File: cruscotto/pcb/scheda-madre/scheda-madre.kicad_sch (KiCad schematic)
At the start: 47 parts, among them J1 Micro-Fit 43045-2400 (D-044), Q1 IPD50N06S4L-12 (60V, da confe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, U1 LM74700-Q1, U2 TPS54360B, U3 LMR36510

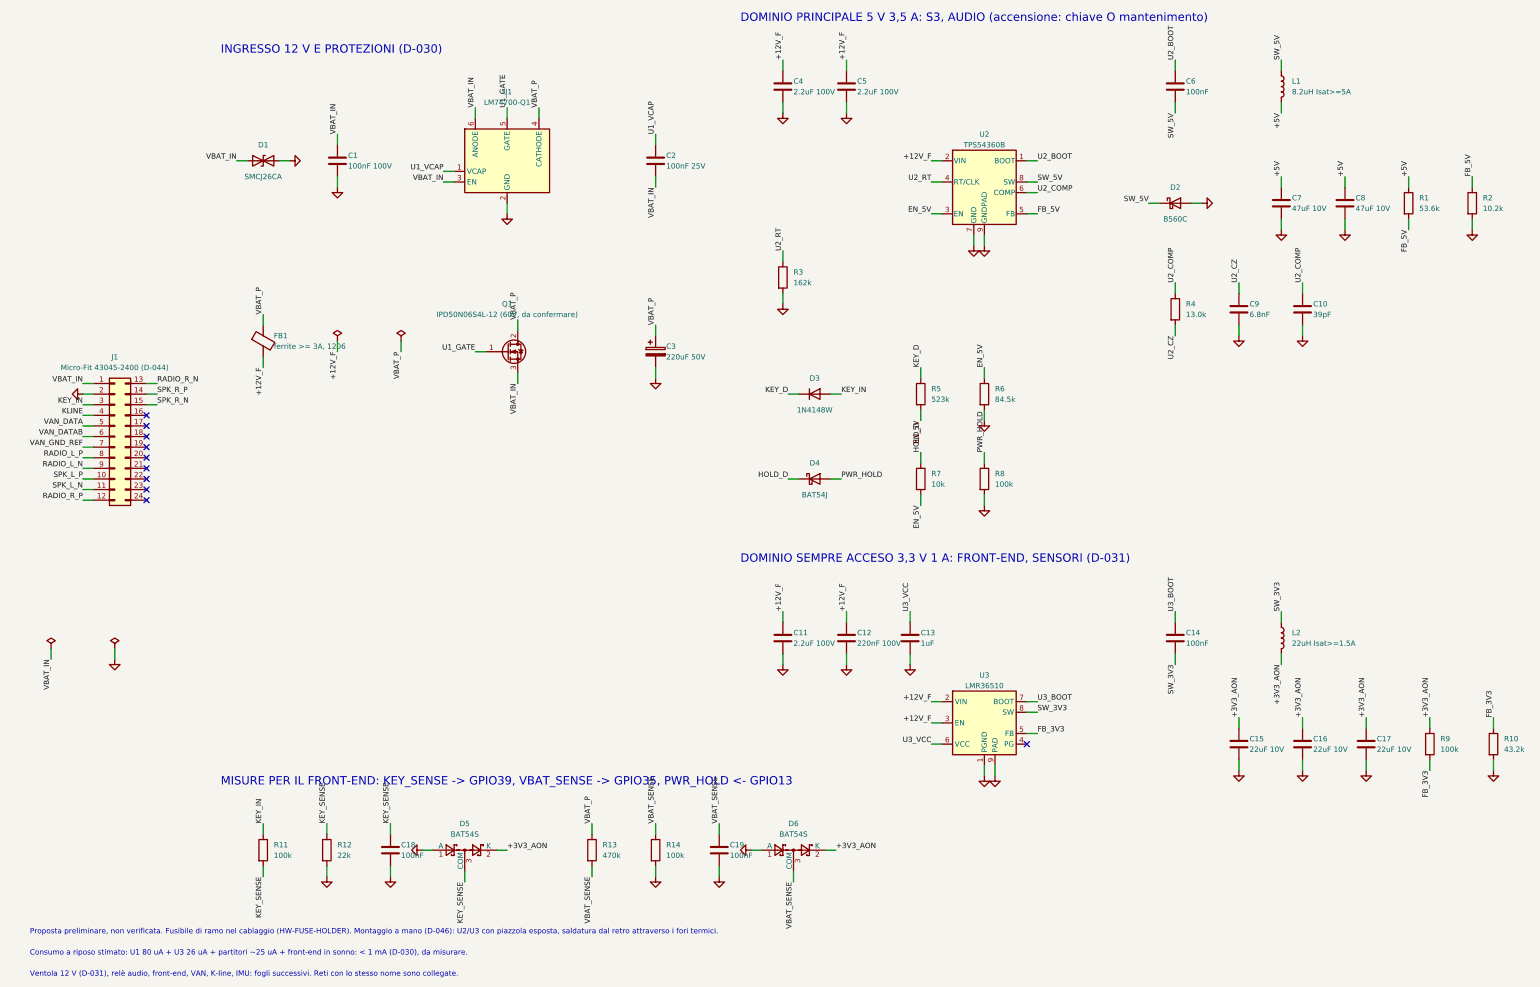
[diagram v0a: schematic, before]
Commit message: feat(schematic): CR-EL-001 rev B with drawn wires inside each block
Labels only for nets leaving a block; the generator checks the KiCad netlist against the intended nets. ERC: 0 errors, 12 expected warnings.

Co-Authored-By: Claude Opus 5.5 <noreply@anthropic.com>
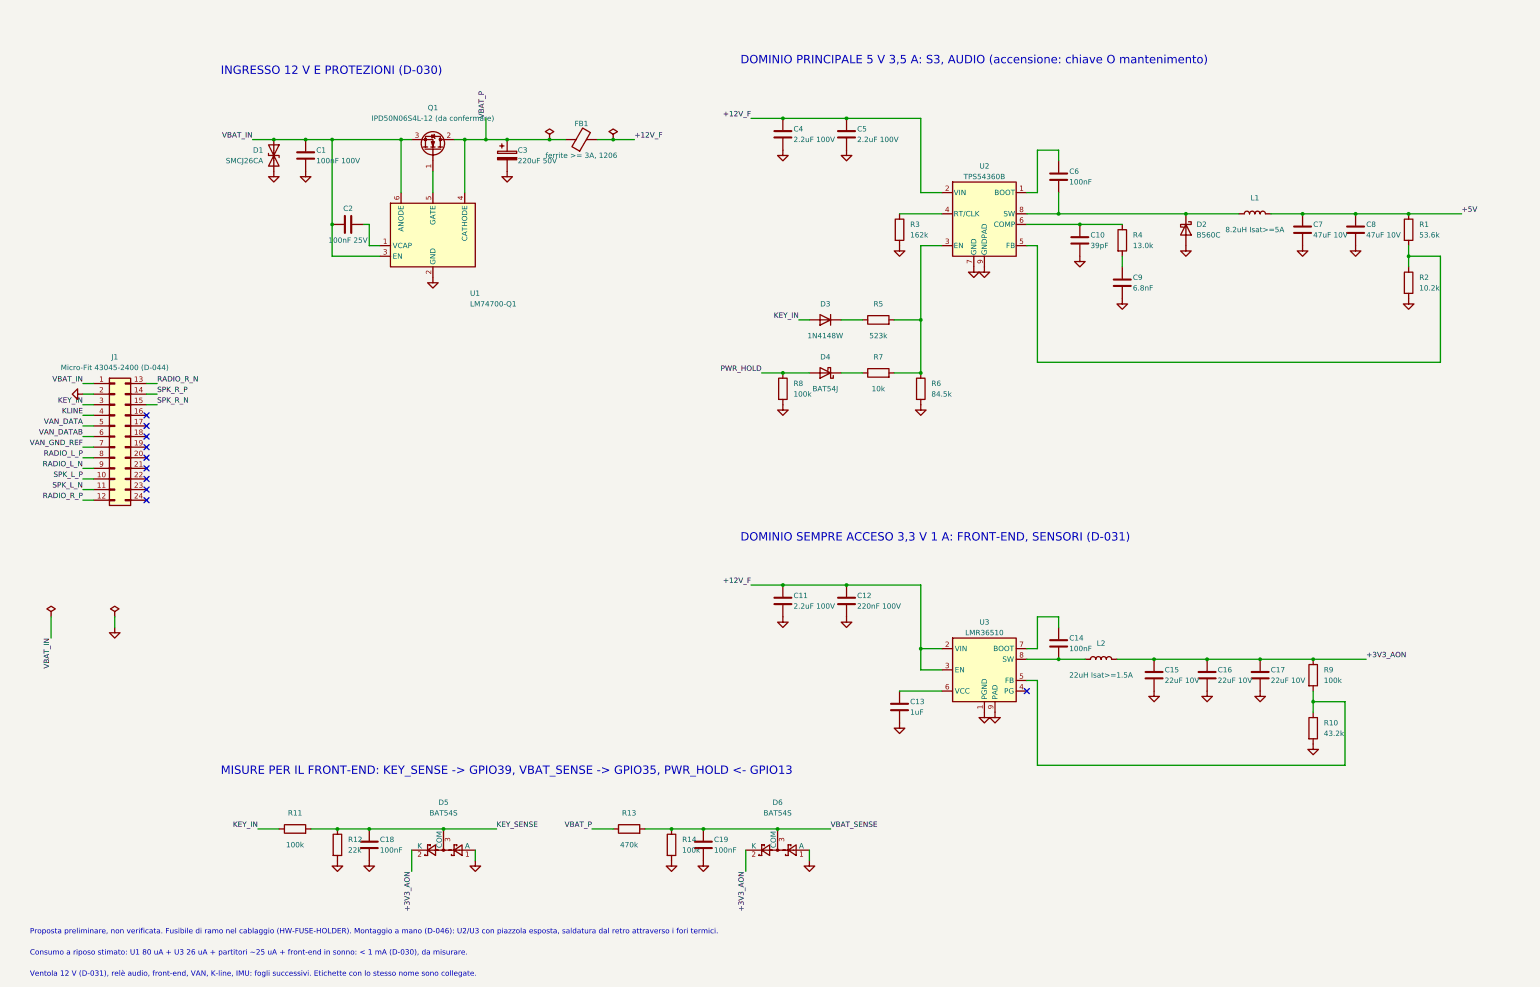
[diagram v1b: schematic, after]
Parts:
- Q1: value IPD50N06S4L-12 (60V, da confermare) -> IPD50N06S4L-12 (da confermare)
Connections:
- net VBAT_IN: now also C2.1; no longer C2.2
- net EN_5V: no longer names the net of R5.2, R6.1, R7.2, U2.3 (EN)
- net FB_3V3: no longer names the net of R10.1, R9.2, U3.5 (FB)
- net FB_5V: no longer names the net of R1.2, R2.1, U2.5 (FB)
- net HOLD_D: no longer names the net of D4.1 (K), R7.1
- net KEY_D: no longer names the net of D3.1 (K), R5.1
- net SW_3V3: no longer names the net of C14.2, L2.1, U3.8 (SW)
- net SW_5V: no longer names the net of C6.2, D2.1 (K), L1.1, U2.8 (SW)
- net U1_GATE: no longer names the net of Q1.1 (G), U1.5 (GATE)
- net U1_VCAP: no longer names the net of U1.1 (VCAP)
- net U1_VCAP: now also C2.2; no longer C2.1
- net U2_BOOT: no longer names the net of C6.1, U2.1 (BOOT)
- net U2_COMP: no longer names the net of C10.1, R4.1, U2.6 (COMP)
- net U2_CZ: no longer names the net of C9.1, R4.2
- net U2_RT: no longer names the net of R3.1, U2.4 (RT/CLK)
- net U3_BOOT: no longer names the net of C14.1, U3.7 (BOOT)
- net U3_VCC: no longer names the net of C13.1, U3.6 (VCC)
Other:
- note added: "Ventola 12 V (D-031), relè audio, front-end, VAN, K-line, IMU: fogli successivi. Etichette con lo stesso nome sono collegate."
- note removed: "Ventola 12 V (D-031), relè audio, front-end, VAN, K-line, IMU: fogli successivi. Reti con lo stesso nome sono collegate."
- moved on the sheet: C1, C10, C11, C12, C13, C14, C15, C16, C17, C18, C19, C2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

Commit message: feat(schematic): front-end sheet C3AI-CR-EL-002 rev A; power sheet rev C as hierarchical root
ESP32-WROOM-32E with bench-only USB-C + CH340C (USB powered), auto-reset, link to the S3, I2C pull-ups, two 100k NTCs, 4-wire fan with high-side switch on GPIO2. Global labels across sheets; the generator checks 81 nets against the KiCad netlist. Inventory: open conflict on factory vs hand mounting of HW-FE-MODULE (D-046).

Co-Authored-By: Claude Opus 5.5 <noreply@anthropic.com>
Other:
- added sheet Front-end (front-end.kicad_sch)

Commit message: feat(schematic): vehicle interface sheet C3AI-CR-EL-003 rev A (K-line and receive-only VAN)
K-line from KL-001 rev F with TVS, series diode and key-referenced threshold; SN65HVD230 receive-only with NUP2105L and its own switched 3.3 V. Generator supports multi-unit symbols and rejects zero-length wires. ERC: 0 errors, 15 expected warnings; 88 nets checked against the KiCad netlist.

Co-Authored-By: Claude Opus 5.5 <noreply@anthropic.com>
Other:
- added sheet Interfacce veicolo (interfacce-veicolo.kicad_sch)
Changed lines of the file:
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@@
 		(instances (project "scheda-madre" (path "/ccee1fe6-cbff-5665-be3b-629f18d22eb3" (page "2"))))
+	)
+	(sheet (at 20.32 213.36) (size 38.1 15.24) (exclude_from_sim no) (in_bom yes) (on_board yes) (dnp no) (stroke (width 0.1524) (type solid)) (fill (color 0 0 0 0.0000))
+		(property "Sheetname" "Interfacce veicolo" (at 20.32 212.66 0) (effects (font (size 1.27 1.27)) (justify left bottom)))
+		(property "Sheetfile" "interfacce-veicolo.kicad_sch" (at 20.32 229.2 0) (effects (font (size 1.27 1.27)) (justify left top)))
+		(instances (project "scheda-madre" (path "/ccee1fe6-cbff-5665-be3b-629f18d22eb3" (page "3"))))
 	)
 	(symbol (lib_id "Connector_Generic:Conn_02x12_Top_Bottom") (at 45.72 116.84 0) (unit 1) (exclude_from_sim no) (in_bom yes) (on_board yes) (dnp no)

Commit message: feat(schematic): sensors and memory sheet C3AI-CR-EL-004 rev A
DIL-24 socket for the STEVAL-MKI196V1 IMU module (I2C 0x6A), optional DS3231SN RTC with non-recharged CR2032, optional MicroSD on the logger SPI pins with pull-ups and switched 3.3 V. Sheet boxes moved to the free area of the root. ERC: 0 errors, 11 expected warnings; 91 nets checked.

Co-Authored-By: Claude Opus 5.5 <noreply@anthropic.com>
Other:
- added sheet Sensori e memoria (sensori-memoria.kicad_sch)
- note added: "Sottofogli: front-end, interfacce veicolo, sensori e memoria. Collegamento con l’S3 e relè audio: da disegnare dopo il rilievo dei connettori della S3. Etichette con lo stesso nome sono collegate."
- note removed: "Ventola 12 V (D-031), relè audio, front-end, VAN, K-line, IMU: fogli successivi. Etichette con lo stesso nome sono collegate."
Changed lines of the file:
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@@
 		(comment 3 "Generato da tools/genera-schema-scheda-madre.py")
 	)
-	(sheet (at 20.32 187.96) (size 38.1 15.24) (exclude_from_sim no) (in_bom yes) (on_board yes) (dnp no) (stroke (width 0.1524) (type solid)) (fill (color 0 0 0 0.0000))
-		(property "Sheetname" "Front-end" (at 20.32 187.26 0) (effects (font (size 1.27 1.27)) (justify left bottom)))
-		(property "Sheetfile" "front-end.kicad_sch" (at 20.32 203.8 0) (effects (font (size 1.27 1.27)) (justify left top)))
+	(sheet (at 279.4 205.74) (size 38.1 12.7) (exclude_from_sim no) (in_bom yes) (on_board yes) (dnp no) (stroke (width 0.1524) (type solid)) (fill (color 0 0 0 0.0000))
+		(property "Sheetname" "Front-end" (at 279.4 205.04 0) (effects (font (size 1.27 1.27)) (justify left bottom)))
+		(property "Sheetfile" "front-end.kicad_sch" (at 279.4 219.04 0) (effects (font (size 1.27 1.27)) (justify left top)))
 		(instances (project "scheda-madre" (path "/ccee1fe6-cbff-5665-be3b-629f18d22eb3" (page "2"))))
 	)
-	(sheet (at 20.32 213.36) (size 38.1 15.24) (exclude_from_sim no) (in_bom yes) (on_board yes) (dnp no) (stroke (width 0.1524) (type solid)) (fill (color 0 0 0 0.0000))
-		(property "Sheetname" "Interfacce veicolo" (at 20.32 212.66 0) (effects (font (size 1.27 1.27)) (justify left bottom)))
-		(property "Sheetfile" "interfacce-veicolo.kicad_sch" (at 20.32 229.2 0) (effects (font (size 1.27 1.27)) (justify left top)))
+	(sheet (at 279.4 228.6) (size 38.1 12.7) (exclude_from_sim no) (in_bom yes) (on_board yes) (dnp no) (stroke (width 0.1524) (type solid)) (fill (color 0 0 0 0.0000))
+		(property "Sheetname" "Interfacce veicolo" (at 279.4 227.9 0) (effects (font (size 1.27 1.27)) (justify left bottom)))
+		(property "Sheetfile" "interfacce-veicolo.kicad_sch" (at 279.4 241.9 0) (effects (font (size 1.27 1.27)) (justify left top)))
 		(instances (project "scheda-madre" (path "/ccee1fe6-cbff-5665-be3b-629f18d22eb3" (page "3"))))
+	)
+	(sheet (at 332.74 205.74) (size 38.1 12.7) (exclude_from_sim no) (in_bom yes) (on_board yes) (dnp no) (stroke (width 0.1524) (type solid)) (fill (color 0 0 0 0.0000))
+		(property "Sheetname" "Sensori e memoria" (at 332.74 205.04 0) (effects (font (size 1.27 1.27)) (justify left bottom)))
+		(property "Sheetfile" "sensori-memoria.kicad_sch" (at 332.74 219.04 0) (effects (font (size 1.27 1.27)) (justify left top)))
+		(instances (project "scheda-madre" (path "/ccee1fe6-cbff-5665-be3b-629f18d22eb3" (page "4"))))
 	)
 	(symbol (lib_id "Connector_Generic:Conn_02x12_Top_Bottom") (at 45.72 116.84 0) (unit 1) (exclude_from_sim no) (in_bom yes) (on_board yes) (dnp no)
@@
 	(text "Proposta preliminare, non verificata. Fusibile di ramo nel cablaggio (HW-FUSE-HOLDER). Montaggio a mano (D-046): U2/U3 con piazzola esposta, saldatura dal retro attraverso i fori termici." (exclude_from_sim no) (at 25.4 236.22 0) (effects (font (size 1.27 1.27)) (justify left bottom)))
 	(text "Consumo a riposo stimato: U1 80 uA + U3 26 uA + partitori ~25 uA + front-end in sonno: < 1 mA (D-030), da misurare." (exclude_from_sim no) (at 25.4 241.3 0) (effects (font (size 1.27 1.27)) (justify left bottom)))
-	(text "Ventola 12 V (D-031), relè audio, front-end, VAN, K-line, IMU: fogli successivi. Etichette con lo stesso nome sono collegate." (exclude_from_sim no) (at 25.4 246.38 0) (effects (font (size 1.27 1.27)) (justify left bottom)))
+	(text "Sottofogli: front-end, interfacce veicolo, sensori e memoria. Collegamento con l’S3 e relè audio: da disegnare dopo il rilievo dei connettori della S3. Etichette con lo stesso nome sono collegate." (exclude_from_sim no) (at 25.4 246.38 0) (effects (font (size 1.27 1.27)) (justify left bottom)))
 	(junction (at 83.82 45.72) (diameter 0) (color 0 0 0 0))
 	(junction (at 91.44 45.72) (diameter 0) (color 0 0 0 0))

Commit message: feat(schematic): S3 link and audio relay sheet C3AI-CR-EL-005 rev A; schematic complete in five sheets
MX1.25 cables to S3 P1/P2/P6 with Schottky on the 5 V feed; two G2RL-2 relays driven by AO3400A from S3 IO13, speakers in series on the S3 output when energised, radio restored at rest. Inventory: S3 connector order, MX1.25 plugs. ERC: 0 errors, 1 warning (VAN ground reference); 95 nets checked.

Co-Authored-By: Claude Opus 5.5 <noreply@anthropic.com>
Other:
- added sheet Collegamento S3 e audio (s3-audio.kicad_sch)
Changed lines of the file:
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@@
 		(instances (project "scheda-madre" (path "/ccee1fe6-cbff-5665-be3b-629f18d22eb3" (page "4"))))
+	)
+	(sheet (at 332.74 228.6) (size 38.1 12.7) (exclude_from_sim no) (in_bom yes) (on_board yes) (dnp no) (stroke (width 0.1524) (type solid)) (fill (color 0 0 0 0.0000))
+		(property "Sheetname" "Collegamento S3 e audio" (at 332.74 227.9 0) (effects (font (size 1.27 1.27)) (justify left bottom)))
+		(property "Sheetfile" "s3-audio.kicad_sch" (at 332.74 241.9 0) (effects (font (size 1.27 1.27)) (justify left top)))
+		(instances (project "scheda-madre" (path "/ccee1fe6-cbff-5665-be3b-629f18d22eb3" (page "5"))))
 	)
 	(symbol (lib_id "Connector_Generic:Conn_02x12_Top_Bottom") (at 45.72 116.84 0) (unit 1) (exclude_from_sim no) (in_bom yes) (on_board yes) (dnp no)

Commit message: feat(bom): power parts verified (Q1, L1, L2, C3), complete purchase list per supplier
- Verification 28/10/2026 from DigiKey parameters and TI pages: IPD50N06S4L-12 (0.06 W at 2.2 A,
  LM74700 gate 12.1-13 V below VGS 16 V), SRR1260-8R2Y (Isat 5.8 A, peak 2.45 A at 2 A load),
  SRN6045TA-220M (Isat 3.3 A, peak 1.17 A), EEU-FR1H221 (about 1 ms ride-through; 17.5 mm tall:
  mount lying down). Schematic EL-001 rev D values and notes, board values updated; DRC unchanged
  (0 errors, 0 unconnected).
- lista-acquisti-scheda-madre.md: LCSC cart (55 lines, 84.52 USD + 13 USD shipping), Farnell quick
  order (16 lines incl. second STEVAL and Micro-Fit bench plug), DigiKey L1 and fan, second MicroSD
  and VAN modules, PCB after Gerbers.

Co-Authored-By: Claude Opus 5.5 <noreply@anthropic.com>
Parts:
- L1: value 8.2uH Isat>=5A -> SRR1260-8R2Y
- L2: value 22uH Isat>=1.5A -> SRN6045TA-220M
- Q1: value IPD50N06S4L-12 (da confermare) -> IPD50N06S4L-12
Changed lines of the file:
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@@
 	(title_block
 		(title "Scheda madre cruscotto C3+AI - alimentazione")
-		(date "2026-10-24")
-		(rev "C")
+		(date "2026-10-28")
+		(rev "D")
 		(company "Cruscotto C3+AI")
-		(comment 1 "C3AI-CR-EL-001 rev C - proposta preliminare, non verificata")
+		(comment 1 "C3AI-CR-EL-001 rev D - proposta preliminare, non verificata")
 		(comment 2 "D-030, D-031, D-044, D-046, D-047, D-048")
 		(comment 3 "Generato da tools/genera-schema-scheda-madre.py")
@@
 	(symbol (lib_id "Transistor_FET:IPD50R380CE") (at 121.92 48.26 90) (mirror y) (unit 1) (exclude_from_sim no) (in_bom yes) (on_board yes) (dnp no)
 		(property "Reference" "Q1" (at 121.92 38.1 90) (effects (font (size 1.27 1.27))))
-		(property "Value" "IPD50N06S4L-12 (da confermare)" (at 121.92 40.64 90) (effects (font (size 1.27 1.27))))
+		(property "Value" "IPD50N06S4L-12" (at 121.92 40.64 90) (effects (font (size 1.27 1.27))))
 		(property "Footprint" "Package_TO_SOT_SMD:TO-252-2" (at 121.92 48.26 0) (hide yes) (effects (font (size 1.27 1.27))))
 		(property "Datasheet" "" (at 121.92 48.26 0) (hide yes) (effects (font (size 1.27 1.27))))
@@
 		(property "Footprint" "Capacitor_THT:CP_Radial_D10.0mm_P5.00mm" (at 139.7 49.53 0) (hide yes) (effects (font (size 1.27 1.27))))
 		(property "Datasheet" "" (at 139.7 49.53 0) (hide yes) (effects (font (size 1.27 1.27))))
-		(property "Description" "Riserva per l'avviamento (-C1), capacità da confermare" (at 139.7 49.53 0) (hide yes) (effects (font (size 1.27 1.27))))
+		(property "Description" "Panasonic EEU-FR1H221, alto 17,5 mm: montarlo coricato; riserva di circa 1 ms, i cali lunghi li reggono i convertitori" (at 139.7 49.53 0) (hide yes) (effects (font (size 1.27 1.27))))
 		(pin "1")
 		(pin "2")
@@
 	(symbol (lib_id "Device:L") (at 318.77 63.5 90) (unit 1) (exclude_from_sim no) (in_bom yes) (on_board yes) (dnp no)
 		(property "Reference" "L1" (at 318.77 59.69 90) (effects (font (size 1.27 1.27))))
-		(property "Value" "8.2uH Isat>=5A" (at 318.77 67.31 90) (effects (font (size 1.27 1.27))))
+		(property "Value" "SRR1260-8R2Y" (at 318.77 67.31 90) (effects (font (size 1.27 1.27))))
 		(property "Footprint" "Inductor_SMD:L_Bourns_SRR1260" (at 318.77 63.5 0) (hide yes) (effects (font (size 1.27 1.27))))
 		(property "Datasheet" "" (at 318.77 63.5 0) (hide yes) (effects (font (size 1.27 1.27))))
-		(property "Description" "Es. Bourns SRR1260-8R2Y, da verificare corrente di saturazione" (at 318.77 63.5 0) (hide yes) (effects (font (size 1.27 1.27))))
+		(property "Description" "Bourns 8,2 uH, Isat 5,8 A, Irms 5,7 A: picco 2,5 A con 2 A di carico, 4 A a 3,5 A (verifica 28/10/2026)" (at 318.77 63.5 0) (hide yes) (effects (font (size 1.27 1.27))))
 		(pin "1")
 		(pin "2")
@@
 	(symbol (lib_id "Device:L") (at 281.94 170.18 90) (unit 1) (exclude_from_sim no) (in_bom yes) (on_board yes) (dnp no)
 		(property "Reference" "L2" (at 281.94 166.37 90) (effects (font (size 1.27 1.27))))
-		(property "Value" "22uH Isat>=1.5A" (at 281.94 173.99 90) (effects (font (size 1.27 1.27))))
+		(property "Value" "SRN6045TA-220M" (at 281.94 173.99 90) (effects (font (size 1.27 1.27))))
 		(property "Footprint" "Inductor_SMD:L_Bourns_SRN6045TA" (at 281.94 170.18 0) (hide yes) (effects (font (size 1.27 1.27))))
 		(property "Datasheet" "" (at 281.94 170.18 0) (hide yes) (effects (font (size 1.27 1.27))))
-		(property "Description" "Es. Bourns SRN6045TA-220M, da verificare" (at 281.94 170.18 0) (hide yes) (effects (font (size 1.27 1.27))))
-		(pin "1")
-		(pin "2")
+		(property "Description" "Bourns 22 uH, Isat 3,3 A, Irms 2,3 A: picco 1,2 A a 1 A di carico (verifica 28/10/2026)" (at 281.94 170.18 0) (hide yes) (effects (font (size 1.27 1.27))))
+		(pin "1")
+		(pin "2")

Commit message: feat(pcb): D-061 contorno v3 (+15 mm in basso) e J1 Micro-Fit verticale 43045-2412
Contorno motherboard_v3.DXF dell'utente (178,7 x 89 mm, fori invariati), J1 verticale
al centro della nuova fascia, piazzamento e sbroglio rifatti: 0 errori DRC, 0 non connessi.
Liste acquisti: J1 da Farnell 1012244, tolto C277384 da LCSC. Ingombro 3D di J1 con spina.

Co-Authored-By: Claude Opus 5.5 <noreply@anthropic.com>
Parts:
- J1: value Micro-Fit 43045-2400 (D-044) -> Micro-Fit 43045-2412 verticale (D-061); footprint Connector_Molex:Molex_Micro-Fit_3.0_43045-2400_2x12_P3.00mm_Horizontal -> Connector_Molex:Molex_Micro-Fit_3.0_43045-2412_2x12_P3.00mm_Vertical
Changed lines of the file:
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@@
 		(title "Scheda madre cruscotto C3+AI - alimentazione")
 		(date "2026-10-28")
-		(rev "D")
+		(rev "E")
 		(company "Cruscotto C3+AI")
-		(comment 1 "C3AI-CR-EL-001 rev D - proposta preliminare, non verificata")
-		(comment 2 "D-030, D-031, D-044, D-046, D-047, D-048")
+		(comment 1 "C3AI-CR-EL-001 rev E - proposta preliminare, non verificata")
+		(comment 2 "D-030, D-031, D-044, D-046, D-047, D-048, D-061")
 		(comment 3 "Generato da tools/genera-schema-scheda-madre.py")
 	)
@@
 	(symbol (lib_id "Connector_Generic:Conn_02x12_Top_Bottom") (at 45.72 116.84 0) (unit 1) (exclude_from_sim no) (in_bom yes) (on_board yes) (dnp no)
 		(property "Reference" "J1" (at 45.72 97.79 0) (effects (font (size 1.27 1.27))))
-		(property "Value" "Micro-Fit 43045-2400 (D-044)" (at 45.72 100.33 0) (effects (font (size 1.27 1.27))))
-		(property "Footprint" "Connector_Molex:Molex_Micro-Fit_3.0_43045-2400_2x12_P3.00mm_Horizontal" (at 45.72 116.84 0) (hide yes) (effects (font (size 1.27 1.27))))
+		(property "Value" "Micro-Fit 43045-2412 verticale (D-061)" (at 45.72 100.33 0) (effects (font (size 1.27 1.27))))
+		(property "Footprint" "Connector_Molex:Molex_Micro-Fit_3.0_43045-2412_2x12_P3.00mm_Vertical" (at 45.72 116.84 0) (hide yes) (effects (font (size 1.27 1.27))))
 		(property "Datasheet" "" (at 45.72 116.84 0) (hide yes) (effects (font (size 1.27 1.27))))
 		(property "Description" "Vie 16-24 riserva; assegnazione bozza (D-044)" (at 45.72 116.84 0) (hide yes) (effects (font (size 1.27 1.27))))
